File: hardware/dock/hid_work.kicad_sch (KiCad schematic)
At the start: 0 parts

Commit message: Dock schematic: review fixes, Pico 2/XIAO socket+pogo mounting
- Cross HID UART TX/RX; split ROLE_STRAP per endpoint
- VBUS sense (GP4) and USB-C CC current sensing (GP26/27) on HID endpoints
- Pogo +5V via TPS2552 enabled by DET, TPD4E1U06 ESD + 1k on pogo lines
- 2x100uF bulk on SYS_5V and keyboard VBUS; 100k EN pull-down
- Remove TPS62162 rail: XIAO from 5V, pull-ups on module 3V3 rails
- Socketed Pico 2 / XIAO footprints with P50-B1 probe holes for USB+SWD
- XIAO SWD header J8; RP2350 reset control of HID/BLE endpoints
- DESIGN.md: UART allocation, power budget, mounting, reset control
- Add .gitignore, custom libraries and datasheets

Co-Authored-By: Claude Opus 5.5 <noreply@anthropic.com>
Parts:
- added A3: RaspberryPi_Pico, dock:RaspberryPi_Pico2_Socket_Pogo, symbol MCU_Module:RaspberryPi_Pico_Extensive
- added C10: 100nF, Capacitor_SMD:C_0805_2012Metric_Pad1.18x1.45mm_HandSolder, symbol Device:C
- added J5: (no value), dock:KLS L-KLS1-5416-L1-01-R, symbol dock_custom:KLS_L-KLS1-5416-L1-01-R
- added J6: Conn_01x05_Pin, Connector_PinHeader_2.54mm:PinHeader_1x05_P2.54mm_Vertical, symbol Connector:Conn_01x05_Pin
- added R14: 330, Resistor_SMD:R_0805_2012Metric_Pad1.20x1.40mm_HandSolder, symbol Device:R
- added R15, R16: 5.1k, Resistor_SMD:R_0805_2012Metric_Pad1.20x1.40mm_HandSolder, symbol Device:R
- added R17, R31, R32, R37: 10k, Resistor_SMD:R_0805_2012Metric_Pad1.20x1.40mm_HandSolder, symbol Device:R
- added R21: 22k, Resistor_SMD:R_0805_2012Metric_Pad1.20x1.40mm_HandSolder, symbol Device:R
- added R22: 33k, Resistor_SMD:R_0805_2012Metric_Pad1.20x1.40mm_HandSolder, symbol Device:R
- added R34: 1k, Resistor_SMD:R_0805_2012Metric_Pad1.20x1.40mm_HandSolder, symbol Device:R
- added U6: TPD2EUSB30, Package_TO_SOT_SMD:Texas_DRT-3, symbol Power_Protection:TPD2EUSB30
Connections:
- new net: A3.D1 (SWCLK), J6.1 (Pin_1)
- new net: A3.D3 (SWDIO), J6.2 (Pin_2)
- new net: C10.1, J5.SH (SHIELD), R14.1
- new net: A3.6 (GPIO4), R21.2, R22.1
- new net: A3.31 (GPIO26_ADC0), R31.1
- new net: A3.32 (GPIO27_ADC1), R32.1
- new net: A3.4 (GPIO2), R17.2
- new net CC1: J5.4 (CC1_A5), R15.1, R31.2
- new net CC2: J5.10 (CC2_B5), R16.1, R32.2
- new net GND: A3.13 (GND), A3.18 (GND), A3.23 (GND), A3.28 (GND), A3.3 (GND), A3.33 (AGND), A3.38 (GND), A3.8 (GND), A3.D2 (GND), A3.TP1 (USB_GND), C10.2, J5.1 (GND_A1_B12), J5.12 (GND_B1_A12), J6.3 (Pin_3), R14.2, R15.2, R16.2, R22.2, U6.3 (GND)
- new net HID_WORK_RUN_CTRL: R34.1
- new net HID_WORK_RX: A3.1 (GPIO0)
- new net HID_WORK_TX: A3.2 (GPIO1)
- new net PICO_3V3: A3.36 (3V3), J6.5 (Pin_5), R17.1, R37.1
- new net RUN: A3.30 (RUN), J6.4 (Pin_4), R34.2, R37.2
- new net SYS_5V: A3.39 (VSYS)
- new net USB_WORK_DM: A3.TP2 (USB_DM), J5.5 (DM_B7), J5.7 (DM_A7), U6.2 (D-)
- new net USB_WORK_DP: A3.TP3 (USB_DP), J5.6 (DP_A6), J5.8 (DP_B6), U6.1 (D+)
- new net WORK_VBUS: J5.11 (VBUS_B4_A9), J5.2 (VBUS_A4_B9), R21.1
- no-connect marks 0 -> 28
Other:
- note added: "Role_Strap"

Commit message: Net classes, project lib tables, docs and datasheets; PCB synced
- Rename USB pairs to *_D_P/*_D_N; add Power and USB net classes
- Project-relative fp-lib-table and new sym-lib-table
- Pico values set to "Raspberry Pi Pico 2"; J1 symbol synced with library
- DESIGN.md/README: Pico 2 x3 + XIAO modules, TPS2116, pogo switch/ESD,
  VBUS/CC sensing, SWD pinout, resolved and open items
- Add TPS2552/2553, TPD2EUSB30 and P50 probe datasheets
- PCB updated from schematic (F8)

Co-Authored-By: Claude Opus 5.5 <noreply@anthropic.com>
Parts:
- A3: value RaspberryPi_Pico -> Raspberry Pi Pico 2
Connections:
- net USB_WORK_DM renamed USB_WORK_D_N
- net USB_WORK_DP renamed USB_WORK_D_P

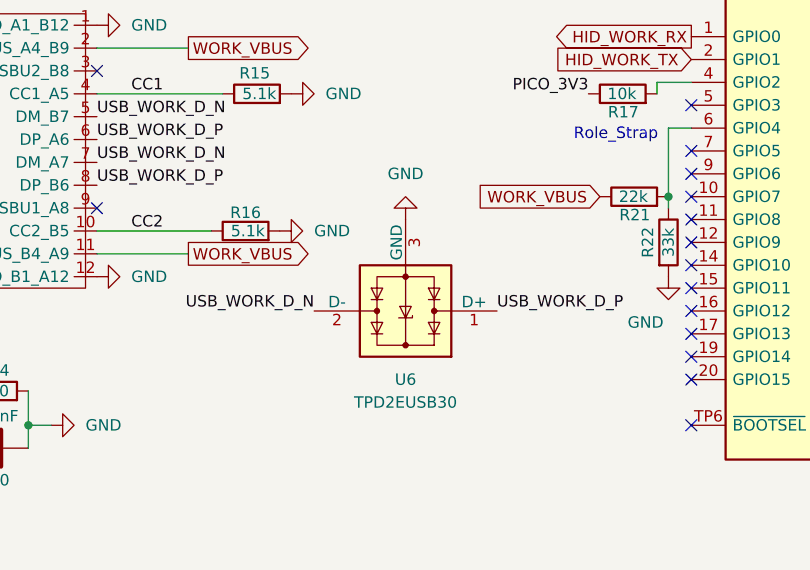
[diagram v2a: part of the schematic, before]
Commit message: USB ESD: TPD2EUSB30 -> TPD4E1U06 on all ports; Pico TP4-6 pads
- U4-U6 now TPD4E1U06 (SOT-23-6, hand-solderable): D+, D-, CC1, CC2
  per port; clamps to GND only, so no back-feed path into PC VBUS
- Keyboard port CC nets named CC1/CC2 (R7/R8 moved along their rows)
- Pico 2 footprint: TP4-TP6 as covered copper-only pads at datasheet
  positions (satisfies F8 pad check, no extra holes)
- Drop unused cached symbols; docs updated; remove TPD2EUSB30 datasheet

Co-Authored-By: Claude Opus 5.5 <noreply@anthropic.com>
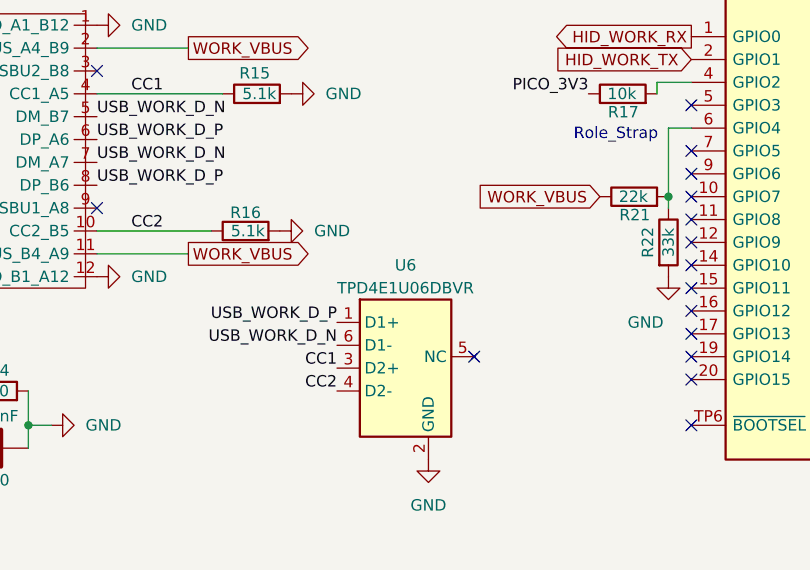
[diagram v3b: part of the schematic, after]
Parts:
- U6: value TPD2EUSB30 -> TPD4E1U06DBVR; footprint Package_TO_SOT_SMD:Texas_DRT-3 -> Package_TO_SOT_SMD:SOT-23-6; symbol Power_Protection:TPD2EUSB30 -> dock_custom:TPD4E1U06DBV
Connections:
- net CC1: now also U6.3 (D2+)
- net CC2: now also U6.4 (D2-)
- net GND: now also U6.2 (GND); no longer U6.3 (GND)
- net USB_WORK_D_N: now also U6.6 (D1-); no longer U6.2 (D-)
- no-connect marks 28 -> 29
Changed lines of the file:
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@@
-		)
-	)
-	(label "USB_WORK_D_N"
-		(at 91.44 116.84 180)
-		(effects
-			(font
-				(size 1.27 1.27)
-			)
-			(justify right bottom)
 		)
 	)
@@
 	(label "CC1"
 		(at 189.23 106.68 0)
-		(effects
-			(font
-				(size 1.27 1.27)
-			)
-			(justify left bottom)
-		)
-	)
-	(label "USB_WORK_D_P"
-		(at 111.76 116.84 0)
 		(effects
 			(font
@@
 	)
 	(symbol
+		(lib_id "Device:R")
+		(at 185.42 116.84 90)
+		(unit 1)
+		(body_style 1)
+		(exclude_from_sim no)
+		(in_bom yes)
+		(on_board yes)
+		(in_pos_files yes)
+		(dnp no)
+		(property "Reference" "R32"
+			(at 187.198 118.872 90)
+			(show_name no)
+			(do_not_autoplace no)
+			(effects
+				(font
+					(size 1.27 1.27)
+				)
+				(justify left)
+			)
+		)
+		(property "Value" "10k"
+			(at 186.944 116.84 90)
+			(show_name no)
+			(do_not_autoplace no)
+			(effects
+				(font
+					(size 1.27 1.27)
+				)
+				(justify left)
+			)
+		)
+		(property "Footprint" "Resistor_SMD:R_0805_2012Metric_Pad1.20x1.40mm_HandSolder"
+			(at 185.42 118.618 90)
+			(hide yes)
+			(show_name no)
+			(do_not_autoplace no)
+			(effects
+				(font
+					(size 1.27 1.27)
+				)
+			)
+		)
+		(property "Datasheet" ""
+			(at 185.42 116.84 0)
+			(hide yes)
+			(show_name no)
+			(do_not_autoplace no)
+			(effects
+				(font
+					(size 1.27 1.27)
+				)
+			)
+		)
+		(property "Description" "Resistor"
+			(at 185.42 116.84 0)
+			(hide yes)
+			(show_name no)
+			(do_not_autoplace no)
+			(effects
+				(font
+					(size 1.27 1.27)
+				)
+			)
+		)
+		(pin "2"
+		)
+		(pin "1"
+		)
+		(instances
+			(project "dock"
+				(path "/b7c42e8e-d530-48de-8d78-684e37659179/22f7f0d8-cebf-4bfb-a7b6-cd9fc1ba10ee"
+					(reference "R32")
+					(unit 1)
+				)
+			)
+		)
+	)
+	(symbol
+		(lib_id "dock_custom:TPD4E1U06DBV")
+		(at 101.6 121.92 0)
+		(unit 1)
+		(body_style 1)
+		(exclude_from_sim no)
+		(in_bom yes)
+		(on_board yes)
+		(in_pos_files yes)
+		(dnp no)
+		(property "Reference" "U6"
+			(at 101.6 111.76 0)
+			(show_name no)
+			(do_not_autoplace no)
+			(effects
+				(font
+					(size 1.27 1.27)
+				)
+			)
+		)
+		(property "Value" "TPD4E1U06DBVR"
+			(at 101.6 114.3 0)
+			(show_name no)
+			(do_not_autoplace no)
+			(effects
+				(font
+					(size 1.27 1.27)
+				)
+			)
+		)
+		(property "Footprint" "Package_TO_SOT_SMD:SOT-23-6"
+			(at 101.6 121.92 0)
+			(hide yes)
+			(show_name no)
+			(do_not_autoplace no)
+			(effects
+				(font
+					(size 1.27 1.27)
+				)
+			)
+		)
+		(property "Datasheet" "https://www.ti.com/lit/ds/symlink/tpd4e1u06.pdf"
+			(at 101.6 121.92 0)
+			(hide yes)
+			(show_name no)
+			(do_not_autoplace no)
+			(effects
+				(font
+					(size 1.27 1.27)
+				)
+			)
+		)
+		(property "Description" "Quad-channel unidirectional ESD protection, 5.5V standoff, SOT-23-6"
+			(at 101.6 121.92 0)
+			(hide yes)
+			(show_name no)
+			(do_not_autoplace no)
+			(effects
+				(font
+					(size 1.27 1.27)
+				)
+			)
+		)
+		(pin "1"
+		)
+		(pin "2"
+		)
+		(pin "3"
+		)
+		(pin "4"
+		)
+		(pin "5"
+		)
+		(pin "6"
+		)
+		(instances
+			(project "dock"
+				(path "/b7c42e8e-d530-48de-8d78-684e37659179/22f7f0d8-cebf-4bfb-a7b6-cd9fc1ba10ee"
+					(reference "U6")
+					(unit 1)
+				)
+			)
+		)
+	)
+	(symbol
 		(lib_id "power:GND")
-		(at 101.6 106.68 180)
+		(at 104.14 133.35 0)
 		(unit 1)
 		(body_style 1)
@@
 		(fields_autoplaced yes)
 		(property "Reference" "#PWR032"
-			(at 101.6 100.33 0)
+			(at 104.14 139.7 0)
 			(hide yes)
 			(show_name no)
@@
 		)
 		(property "Value" "GND"
-			(at 101.6 101.6 0)
+			(at 104.14 138.43 0)
 			(show_name no)
 			(do_not_autoplace no)
@@
 		)
 		(property "Footprint" ""
-			(at 101.6 106.68 0)
+			(at 104.14 133.35 0)
 			(hide yes)
 			(show_name no)
@@
 		)
 		(property "Datasheet" ""
-			(at 101.6 106.68 0)
+			(at 104.14 133.35 0)
 			(hide yes)
 			(show_name no)
@@
 		)
 		(property "Description" "Power symbol creates a global label with name \"GND\" , ground"
-			(at 101.6 106.68 0)
+			(at 104.14 133.35 0)
 			(hide yes)
 			(show_name no)
@@
 		)
 	)
-	(symbol
-		(lib_id "Power_Protection:TPD2EUSB30")
-		(at 101.6 116.84 180)
-		(unit 1)
-		(body_style 1)
-		(exclude_from_sim no)
-		(in_bom yes)
-		(on_board yes)
-		(in_pos_files yes)
-		(dnp no)
-		(fields_autoplaced yes)
-		(property "Reference" "U6"
-			(at 101.6 124.46 0)
-			(show_name no)
-			(do_not_autoplace no)
-			(effects
-				(font
-					(size 1.27 1.27)
-				)
-			)
-		)
-		(property "Value" "TPD2EUSB30"
-			(at 101.6 127 0)
-			(show_name no)
-			(do_not_autoplace no)
-			(effects
-				(font
-					(size 1.27 1.27)
-				)
-			)
-		)
-		(property "Footprint" "Package_TO_SOT_SMD:Texas_DRT-3"
-			(at 120.65 109.22 0)
-			(hide yes)
-			(show_name no)
-			(do_not_autoplace no)
-			(effects
-				(font
-					(size 1.27 1.27)
-				)
-			)
-		)
-		(property "Datasheet" "http://www.ti.com/lit/ds/symlink/tpd2eusb30a.pdf"
-			(at 101.6 116.84 0)
-			(hide yes)
-			(show_name no)
-			(do_not_autoplace no)
-			(effects
-				(font
-					(size 1.27 1.27)
-				)
-			)
-		)
-		(property "Description" "2-Channel ESD Protection for Super-Speed USB 3.0 Interface, DRT-3"
-			(at 101.6 116.84 0)
-			(hide yes)
-			(show_name no)
-			(do_not_autoplace no)
-			(effects
-				(font
-					(size 1.27 1.27)
-				)
-			)
-		)
-		(pin "1"
-		)
-		(pin "2"
-		)
-		(pin "3"
-		)
-		(instances
-			(project "dock"
-				(path "/b7c42e8e-d530-48de-8d78-684e37659179/22f7f0d8-cebf-4bfb-a7b6-cd9fc1ba10ee"
-					(reference "U6")
-					(unit 1)
-				)
-			)
-		)
-	)
-	(symbol
-		(lib_id "Device:R")
-		(at 185.42 116.84 90)
-		(unit 1)
-		(body_style 1)
-		(exclude_from_sim no)
-		(in_bom yes)
-		(on_board yes)
-		(in_pos_files yes)
-		(dnp no)
-		(property "Reference" "R32"
-			(at 187.198 118.872 90)
-			(show_name no)
-			(do_not_autoplace no)
-			(effects
-				(font
-					(size 1.27 1.27)
-				)
-				(justify left)
-			)
-		)
-		(property "Value" "10k"
-			(at 186.944 116.84 90)
-			(show_name no)
-			(do_not_autoplace no)
-			(effects
-				(font
-					(size 1.27 1.27)
-				)
-				(justify left)
-			)
-		)
-		(property "Footprint" "Resistor_SMD:R_0805_2012Metric_Pad1.20x1.40mm_HandSolder"
-			(at 185.42 118.618 90)
-			(hide yes)
-			(show_name no)
-			(do_not_autoplace no)
-			(effects
-				(font
-					(size 1.27 1.27)
-				)
-			)
-		)
-		(property "Datasheet" ""
-			(at 185.42 116.84 0)
-			(hide yes)
-			(show_name no)
-			(do_not_autoplace no)
-			(effects
-				(font
-					(size 1.27 1.27)
-				)
-			)
-		)
-		(property "Description" "Resistor"
-			(at 185.42 116.84 0)
-			(hide yes)
-			(show_name no)
-			(do_not_autoplace no)
-			(effects
-				(font
-					(size 1.27 1.27)
-				)
-			)
-		)
-		(pin "2"
-		)
-		(pin "1"
-		)
-		(instances
-			(project "dock"
-				(path "/b7c42e8e-d530-48de-8d78-684e37659179/22f7f0d8-cebf-4bfb-a7b6-cd9fc1ba10ee"
-					(reference "R32")
-					(unit 1)
-				)
-			)
-		)
-	)
+	(no_connect
+		(at 109.22 121.92)
+	)
+	(label "USB_WORK_D_P"
+		(at 93.98 118.11 180)
+		(effects
+			(font
+				(size 1.27 1.27)
+			)
+			(justify right bottom)
+		)
+	)
+	(label "USB_WORK_D_N"
+		(at 93.98 120.65 180)
+		(effects
+			(font
+				(size 1.27 1.27)
+			)
+			(justify right bottom)
+		)
+	)
+	(label "CC1"
+		(at 93.98 123.19 180)
+		(effects
+			(font
+				(size 1.27 1.27)
+			)
+			(justify right bottom)
+		)
+	)
+	(label "CC2"
+		(at 93.98 125.73 180)
+		(effects
+			(font
+				(size 1.27 1.27)
+			)
+			(justify right bottom)
+		)
+	)

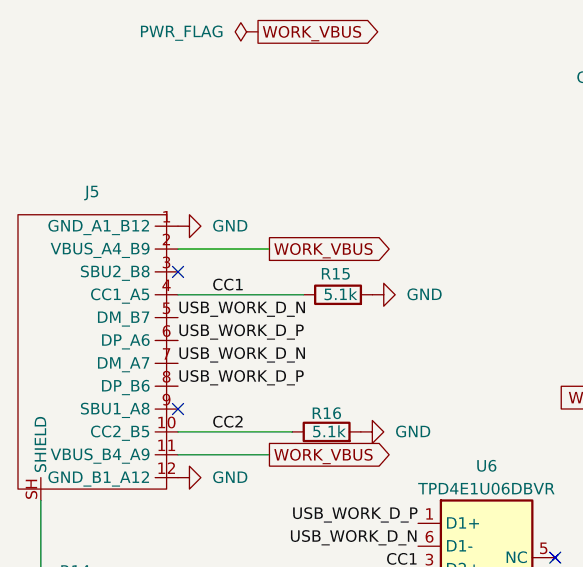
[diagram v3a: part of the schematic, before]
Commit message: Set part values; drop unused Seeed library; add Panasonic FK datasheet
- U3 value TPS2553DBVR, J1/J4/J5 value L-KLS1-5416-L1-01-R
- Remove hardware/libraries/seed-xio and its fp-lib-table entry (XIAO now
  uses dock:XIAO_nRF52840_Socket_Pogo; nothing references xiao:)
- Add Panasonic FK series catalog (C13-C16, EEE-FK1E101XP)

Co-Authored-By: Claude Opus 5.5 <noreply@anthropic.com>
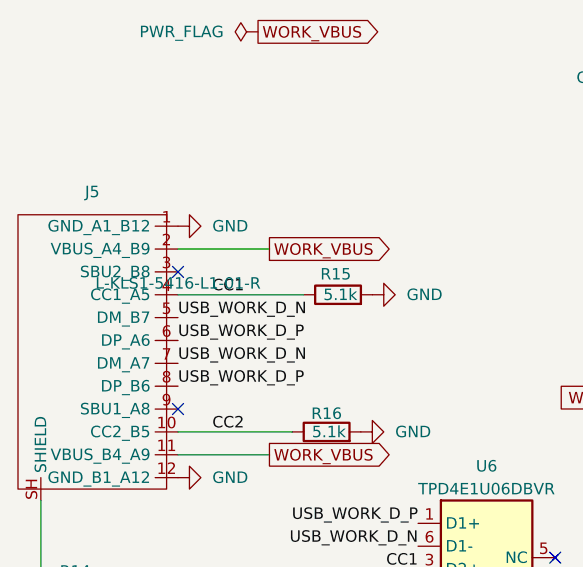
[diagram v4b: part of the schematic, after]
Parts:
- J5: value (none) -> L-KLS1-5416-L1-01-R
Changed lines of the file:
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@@
 			)
 		)
-		(property "Value" ""
+		(property "Value" "L-KLS1-5416-L1-01-R"
 			(at 67.31 91.44 0)
 			(show_name no)
